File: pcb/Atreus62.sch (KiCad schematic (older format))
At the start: 125 parts, among them SW1 SWITCH_PUSH, SW10 SWITCH_PUSH, SW11 SWITCH_PUSH, SW12 SWITCH_PUSH, SW13 SWITCH_PUSH, SW14 SWITCH_PUSH, SW15 SWITCH_PUSH, SW16 SWITCH_PUSH, SW17 SWITCH_PUSH, SW18 SWITCH_PUSH, SW19 SWITCH_PUSH, SW2 SWITCH_PUSH, SW20 SWITCH_PUSH, SW21 SWITCH_PUSH, SW22 SWITCH_PUSH, SW23 SWITCH_PUSH, SW24 SWITCH_PUSH, SW25 SWITCH_PUSH, SW26 SWITCH_PUSH, SW27 SWITCH_PUSH, SW28 SWITCH_PUSH, SW29 SWITCH_PUSH, SW3 SWITCH_PUSH, SW30 SWITCH_PUSH, SW31 SWITCH_PUSH, SW32 SWITCH_PUSH, SW33 SWITCH_PUSH, SW34 SWITCH_PUSH, SW35 SWITCH_PUSH, SW36 SWITCH_PUSH, SW37 SWITCH_PUSH, SW38 SWITCH_PUSH, SW39 SWITCH_PUSH, SW4 SWITCH_PUSH, SW40 SWITCH_PUSH, SW41 SWITCH_PUSH, SW42 SWITCH_PUSH, SW43 SWITCH_PUSH, SW44 SWITCH_PUSH, SW45 SWITCH_PUSH, SW46 SWITCH_PUSH, SW47 SWITCH_PUSH, SW48 SWITCH_PUSH, SW49 SWITCH_PUSH, SW5 SWITCH_PUSH, SW50 SWITCH_PUSH, SW51 SWITCH_PUSH, SW52 SWITCH_PUSH, SW53 SWITCH_PUSH, SW54 SWITCH_PUSH, SW55 SWITCH_PUSH, SW56 SWITCH_PUSH, SW57 SWITCH_PUSH, SW58 SWITCH_PUSH, SW59 SWITCH_PUSH, SW6 SWITCH_PUSH, SW60 SWITCH_PUSH, SW61 SWITCH_PUSH, SW62 SWITCH_PUSH, SW7 SWITCH_PUSH, SW8 SWITCH_PUSH, SW9 SWITCH_PUSH, U1 ARDUINO_PRO_MICRO

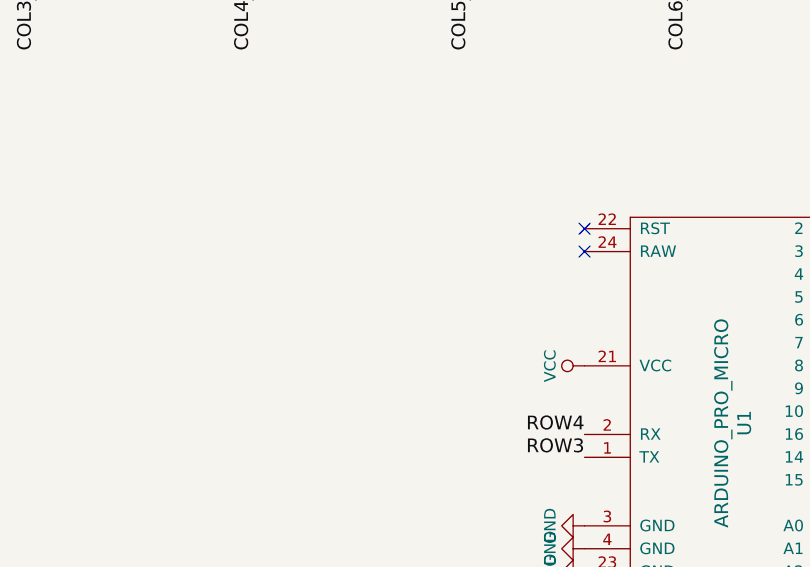
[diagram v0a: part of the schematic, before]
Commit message: Adding reset switch to PCB
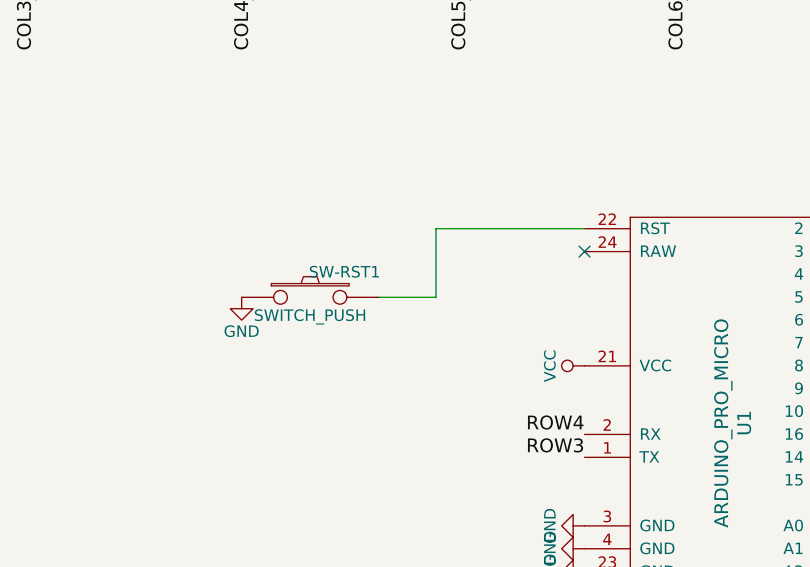
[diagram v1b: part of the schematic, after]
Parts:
- added SW-RST1: SWITCH_PUSH, Buttons_Switches_SMD:SW_SPST_B3U-1000P, symbol SWITCH_PUSH
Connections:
- net GND: now also SW-RST1.1
- net at U1.22 (RST): now also SW-RST1.2
- no-connect marks 2 -> 1
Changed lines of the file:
@@
 	0    -1   -1   0
 $EndComp
-NoConn ~ 6300 5600
 NoConn ~ 6300 5700
 $Comp
@@
 	0    1    1    0
 $EndComp
+$Comp
+L SWITCH_PUSH SW-RST1
+U 1 1 5839BFF0
+P 5100 5900
+F 0 "SW-RST1" H 5250 6010 50  0000 C CNN
+F 1 "SWITCH_PUSH" H 5100 5820 50  0000 C CNN
+F 2 "Buttons_Switches_SMD:SW_SPST_B3U-1000P" H 5100 5900 60  0001 C CNN
+F 3 "" H 5100 5900 60  0001 C CNN
+	1    5100 5900
+	1    0    0    -1
+$EndComp
+Wire Wire Line
+	5400 5900 5650 5900
+Wire Wire Line
+	5650 5900 5650 5600
+Wire Wire Line
+	5650 5600 6300 5600
+$Comp
+L GND #PWR05
+U 1 1 583A2352
+P 4800 5900
+F 0 "#PWR05" H 4800 5650 50  0001 C CNN
+F 1 "GND" H 4800 5750 50  0000 C CNN
+F 2 "" H 4800 5900 50  0000 C CNN
+F 3 "" H 4800 5900 50  0000 C CNN
+	1    4800 5900
+	1    0    0    -1
+$EndComp
 $EndSCHEMATC

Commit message: Merging in changes from NaCly
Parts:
- D1, D10, D11, D12, D13, D14, D15, D16, D17, D18, D19, D2, D20, D21, D22, D23, D24, D25, D26, D27, D28, D29, D3, D30, D31, D32, D33, D34, D35, D36, D37, D38, D39, D4, D40, D41, D42, D43, D44, D45, D46, D47, D48, D49, D5, D50, D51, D52, D53, D54, D55, D56, D57, D58, D59, D6, D60, D61, D62, D7, D8, D9: footprint Diodes_SMD:SOD-123 -> footprints:Diode-Hybrid-Back; symbol DIODE -> UA62-rescue:DIODE-components
- SW-RST1: symbol SWITCH_PUSH -> UA62-rescue:SWITCH_PUSH-components
- SW1, SW10, SW11, SW12, SW13, SW14, SW15, SW16, SW17, SW18, SW19, SW2, SW20, SW21, SW22, SW23, SW24, SW25, SW26, SW27, SW28, SW29, SW3, SW30, SW31, SW32, SW33, SW34, SW35, SW36, SW37, SW38, SW39, SW4, SW40, SW41, SW42, SW43, SW44, SW45, SW46, SW47, SW48, SW49, SW5, SW50, SW51, SW52, SW53, SW54, SW55, SW56, SW57, SW58, SW59, SW6, SW60, SW61, SW62, SW7, SW8, SW9: footprint footprints:CHERRY_PCB_100H -> footprints:MX-Alps-Choc-1U-NoLED; symbol SWITCH_PUSH -> UA62-rescue:SWITCH_PUSH-components
- U1: symbol ARDUINO_PRO_MICRO -> UA62-rescue:ARDUINO_PRO_MICRO-generic_kbd-cache
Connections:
- wire segments 331 -> 437
